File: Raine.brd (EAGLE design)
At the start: 307.5 x 100.4 mm, 172 parts, among them J1 USB-C-M12-TYPE-C-31-M12, SW1 TL3342F160QG/TR, SW2 TL3342F160QG/TR, U2 ATMEGA32U4-AUR44ML-L

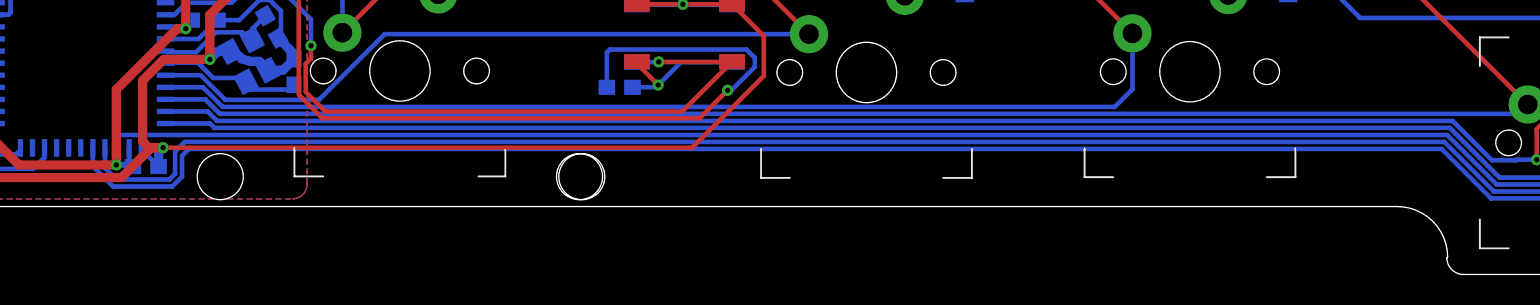
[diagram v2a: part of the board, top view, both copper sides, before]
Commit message: Update for JLCPCB
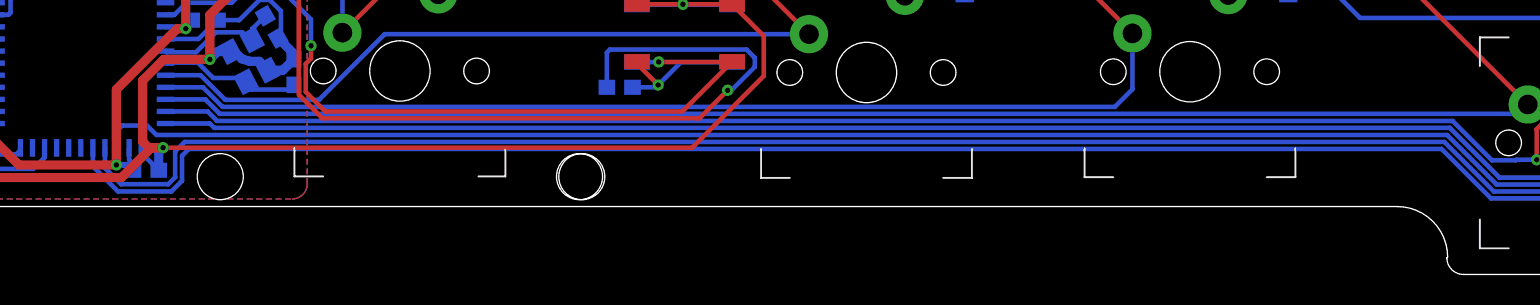
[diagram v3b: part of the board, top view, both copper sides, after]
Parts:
- moved C5 0.25 mm to (123.3, -92.1)
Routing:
- net COL14: track 220.9 -> 221.7 mm
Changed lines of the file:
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@@
 <attribute name="VALUE" x="112.6844125" y="-81.272134375" size="0.6008875" layer="28" rot="MR315"/>
 </element>
-<element name="C5" library="Keyboard_parts" library_urn="urn:adsk.eagle:library:6380734" package="CAPC1608X90" package3d_urn="urn:adsk.eagle:package:6154640/2" value="0.1" x="123.305" y="-91.85" smashed="yes" rot="MR180">
-<attribute name="AVAILABILITY" value="Unavailable" x="113.305" y="-81.85" size="1.778" layer="28" rot="MR180" display="off"/>
-<attribute name="DESCRIPTION" value=" Cap Cer 10000pf 10v 10% X7r 0603 " x="113.305" y="-81.85" size="1.778" layer="28" rot="MR180" display="off"/>
-<attribute name="MF" value="AVX" x="113.305" y="-81.85" size="1.778" layer="28" rot="MR180" display="off"/>
-<attribute name="MP" value="0603ZC103KAJ2A" x="113.305" y="-81.85" size="1.778" layer="28" rot="MR180" display="off"/>
-<attribute name="NAME" x="121.56403125" y="-92.78821875" size="0.602065625" layer="26" rot="MR180"/>
-<attribute name="PACKAGE" value="0603 AVX" x="113.305" y="-81.85" size="1.778" layer="28" rot="MR180" display="off"/>
-<attribute name="PRICE" value="None" x="113.305" y="-81.85" size="1.778" layer="28" rot="MR180" display="off"/>
-<attribute name="VALUE" x="121.567440625" y="-90.34276875" size="0.6008875" layer="28" rot="MR180"/>
+<element name="C5" library="Keyboard_parts" library_urn="urn:adsk.eagle:library:6380734" package="CAPC1608X90" package3d_urn="urn:adsk.eagle:package:6154640/2" value="0.1" x="123.313" y="-92.098" smashed="yes" rot="MR180">
+<attribute name="AVAILABILITY" value="Unavailable" x="113.313" y="-82.098" size="1.778" layer="28" rot="MR180" display="off"/>
+<attribute name="DESCRIPTION" value=" Cap Cer 10000pf 10v 10% X7r 0603 " x="113.313" y="-82.098" size="1.778" layer="28" rot="MR180" display="off"/>
+<attribute name="MF" value="AVX" x="113.313" y="-82.098" size="1.778" layer="28" rot="MR180" display="off"/>
+<attribute name="MP" value="0603ZC103KAJ2A" x="113.313" y="-82.098" size="1.778" layer="28" rot="MR180" display="off"/>
+<attribute name="NAME" x="121.57203125" y="-93.03621875" size="0.602065625" layer="26" rot="MR180"/>
+<attribute name="PACKAGE" value="0603 AVX" x="113.313" y="-82.098" size="1.778" layer="28" rot="MR180" display="off"/>
+<attribute name="PRICE" value="None" x="113.313" y="-82.098" size="1.778" layer="28" rot="MR180" display="off"/>
+<attribute name="VALUE" x="121.575440625" y="-90.59076875" size="0.6008875" layer="28" rot="MR180"/>
 </element>
 <element name="C6" library="Keyboard_parts" library_urn="urn:adsk.eagle:library:6380734" package="CAPC1608X90" package3d_urn="urn:adsk.eagle:package:6154640/2" value="0.1" x="127.2" y="-82.15" smashed="yes" rot="MR180">
@@
 <wire x1="118.2" y1="-78.48105" x2="117.8452" y2="-78.12625" width="0.3048" layer="16"/>
 <wire x1="117.8452" y1="-78.12625" x2="117.8452" y2="-76.3048" width="0.3048" layer="16"/>
-<wire x1="124.155" y1="-91.85" x2="123" y2="-90.695" width="0.3048" layer="16"/>
-<wire x1="123" y1="-90.6134" x2="123" y2="-90.695" width="0.3048" layer="16"/>
+<wire x1="124.163" y1="-92.098" x2="123" y2="-90.935" width="0.3048" layer="16"/>
+<wire x1="123" y1="-90.6134" x2="123" y2="-90.935" width="0.3048" layer="16"/>
 <wire x1="128.05" y1="-82.15" x2="126.8" y2="-83.4" width="0.3048" layer="16"/>
 <wire x1="126.8" y1="-83.4" x2="124.6134" y2="-83.4" width="0.3048" layer="16"/>
@@
 <wire x1="111.17744375" y1="-92.57744375" x2="121.70399375" y2="-92.57744375" width="0.6096" layer="1"/>
 <wire x1="109.05" y1="-90.45" x2="111.17744375" y2="-92.57744375" width="0.6096" layer="1"/>
-<wire x1="124.45" y1="-90.6" x2="124.155" y2="-90.895" width="0.6096" layer="16"/>
-<wire x1="124.155" y1="-90.895" x2="124.155" y2="-91.85" width="0.6096" layer="16"/>
+<wire x1="124.45" y1="-90.6" x2="124.163" y2="-90.887" width="0.6096" layer="16"/>
+<wire x1="124.163" y1="-90.887" x2="124.163" y2="-92.098" width="0.6096" layer="16"/>
 <wire x1="123.1" y1="-86.15" x2="123.1" y2="-90.2" width="0.6096" layer="1"/>
 <wire x1="124.45" y1="-90.6" x2="123.5" y2="-90.6" width="0.6096" layer="1"/>
@@
 <wire x1="122.2" y1="-90.6134" x2="122.2" y2="-91.4" width="0.3048" layer="16"/>
 <wire x1="122.2" y1="-91.4" x2="122.4" y2="-91.6" width="0.3048" layer="16"/>
-<wire x1="122.3025" y1="-91.6975" x2="122.455" y2="-91.85" width="0.3048" layer="16"/>
+<wire x1="122.1825" y1="-91.8175" x2="122.463" y2="-92.098" width="0.3048" layer="16"/>
 <wire x1="124.6134" y1="-82.6" x2="125.9" y2="-82.6" width="0.3048" layer="16"/>
 <wire x1="125.9" y1="-82.6" x2="126.35" y2="-82.15" width="0.3048" layer="16"/>
@@
 <via x="121.35795625" y="-91.74204375" extent="1-16" drill="0.35"/>
 <wire x1="121.35795625" y1="-91.74204375" x2="122.25795625" y2="-91.74204375" width="0.4064" layer="16"/>
-<wire x1="122.25795625" y1="-91.74204375" x2="122.3025" y2="-91.6975" width="0.4064" layer="16"/>
-<wire x1="122.3025" y1="-91.6975" x2="122.4" y2="-91.6" width="0.4064" layer="16"/>
+<wire x1="122.1825" y1="-91.8175" x2="122.25795625" y2="-91.74204375" width="0.4064" layer="16"/>
+<wire x1="122.25795625" y1="-91.74204375" x2="122.4" y2="-91.6" width="0.4064" layer="16"/>
 <via x="125.95" y="-82.717" extent="1-16" drill="0.35"/>
 <wire x1="126.35" y1="-82.15" x2="126.35" y2="-82.317" width="0.4064" layer="16"/>
@@
 <wire x1="295.57" y1="-63.98" x2="295.57" y2="-82.98" width="0.3048" layer="1"/>
 <contactref element="U2" pad="27"/>
-<wire x1="119.8" y1="-91.83658125" x2="121.13541875" y2="-93.172" width="0.3048" layer="16"/>
+<wire x1="119.8" y1="-91.83658125" x2="121.46341875" y2="-93.5" width="0.3048" layer="16"/>
 <wire x1="119.8" y1="-90.6134" x2="119.8" y2="-91.83658125" width="0.3048" layer="16"/>
-<wire x1="121.13541875" y1="-93.172" x2="125.05563125" y2="-93.172" width="0.3048" layer="16"/>
-<wire x1="125.05563125" y1="-93.172" x2="125.7072" y2="-92.52043125" width="0.3048" layer="16"/>
+<wire x1="121.46341875" y1="-93.5" x2="124.99963125" y2="-93.5" width="0.3048" layer="16"/>
+<wire x1="124.99963125" y1="-93.5" x2="125.7072" y2="-92.79243125" width="0.3048" layer="16"/>
 <wire x1="125.7072" y1="-91.136" x2="126.16" y2="-90.6832" width="0.3048" layer="16"/>
-<wire x1="125.7072" y1="-92.52043125" x2="125.7072" y2="-91.136" width="0.3048" layer="16"/>
+<wire x1="125.7072" y1="-92.79243125" x2="125.7072" y2="-91.136" width="0.3048" layer="16"/>
 <wire x1="209.146875" y1="-90.6832" x2="212.420075" y2="-93.9564" width="0.3048" layer="16"/>
 <wire x1="212.420075" y1="-93.9564" x2="262.09018125" y2="-93.9564" width="0.3048" layer="16"/>
@@
 <contactref element="U2" pad="26"/>
 <wire x1="120.6" y1="-90.6134" x2="120.6" y2="-91.95" width="0.3048" layer="16"/>
-<wire x1="120.6" y1="-91.95" x2="121.3598" y2="-92.7098" width="0.3048" layer="16"/>
-<wire x1="121.3598" y1="-92.7098" x2="124.87125" y2="-92.7098" width="0.3048" layer="16"/>
+<wire x1="120.6" y1="-91.95" x2="121.6718" y2="-93.0218" width="0.3048" layer="16"/>
+<wire x1="121.6718" y1="-93.0218" x2="124.79125" y2="-93.0218" width="0.3048" layer="16"/>
 <wire x1="209.33125625" y1="-90.221" x2="212.60945625" y2="-93.4992" width="0.3048" layer="16"/>
 <wire x1="209.33125625" y1="-90.221" x2="125.879" y2="-90.221" width="0.3048" layer="16"/>
@@
 <wire x1="212.60945625" y1="-93.4992" x2="261.9008" y2="-93.4992" width="0.3048" layer="16"/>
 <wire x1="261.9008" y1="-93.4992" x2="272.42" y2="-82.98" width="0.3048" layer="16"/>
-<wire x1="124.87125" y1="-92.7098" x2="125.25" y2="-92.33105" width="0.3048" layer="16"/>
-<wire x1="125.25" y1="-92.33105" x2="125.25" y2="-90.85" width="0.3048" layer="16"/>
+<wire x1="124.79125" y1="-93.0218" x2="125.25" y2="-92.56305" width="0.3048" layer="16"/>
+<wire x1="125.25" y1="-92.56305" x2="125.25" y2="-90.85" width="0.3048" layer="16"/>
 <wire x1="125.25" y1="-90.85" x2="125.879" y2="-90.221" width="0.3048" layer="16"/>
 </signal>
@@
 <wire x1="257.57" y1="-83.03" x2="252.86" y2="-87.74" width="0.3048" layer="1"/>
 <contactref element="U2" pad="25"/>
-<wire x1="121.4" y1="-90.6134" x2="121.4" y2="-89.95" width="0.3048" layer="16"/>
-<wire x1="121.5906" y1="-89.7594" x2="209.5162375" y2="-89.7594" width="0.3048" layer="16"/>
-<wire x1="121.4" y1="-89.95" x2="121.5906" y2="-89.7594" width="0.3048" layer="16"/>
+<wire x1="124.01" y1="-89.7594" x2="209.5162375" y2="-89.7594" width="0.3048" layer="16"/>
 <wire x1="209.5162375" y1="-89.7594" x2="212.7988375" y2="-93.042" width="0.3048" layer="16"/>
 <wire x1="252.86" y1="-91.94" x2="252.86" y2="-87.74" width="0.3048" layer="16"/>
 <wire x1="212.7988375" y1="-93.042" x2="251.758" y2="-93.042" width="0.3048" layer="16"/>
 <wire x1="251.758" y1="-93.042" x2="252.86" y2="-91.94" width="0.3048" layer="16"/>
+<wire x1="123.3856" y1="-89.135" x2="124.01" y2="-89.7594" width="0.3048" layer="16"/>
+<wire x1="121.4" y1="-90.6134" x2="121.4" y2="-89.485" width="0.3048" layer="16"/>
+<wire x1="121.4" y1="-89.485" x2="121.75" y2="-89.135" width="0.3048" layer="16"/>
+<wire x1="121.75" y1="-89.135" x2="123.3856" y2="-89.135" width="0.3048" layer="16"/>
 </signal>
 <signal name="COL10" airwireshidden="yes">
